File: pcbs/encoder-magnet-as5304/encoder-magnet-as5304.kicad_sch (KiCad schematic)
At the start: 14 parts, among them J1 Conn_01x05, Q1 BC807-40LWX, U1 AS5304

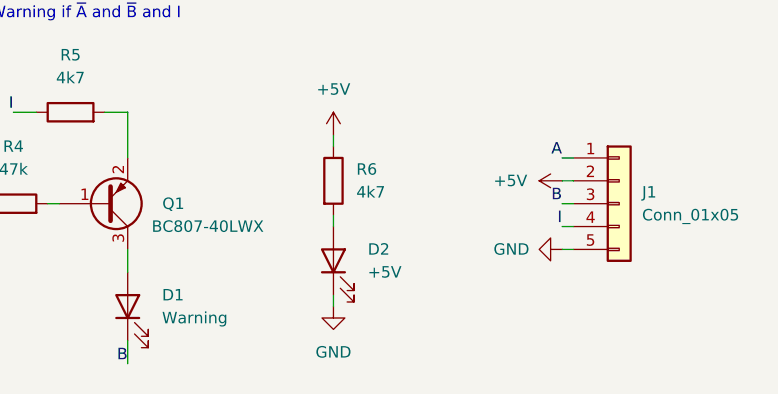
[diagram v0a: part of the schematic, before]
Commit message: Fix AS5304 board dimensions
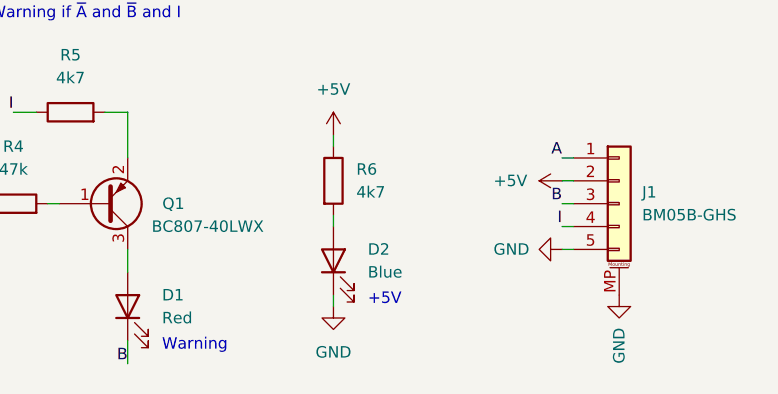
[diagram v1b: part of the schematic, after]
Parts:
- D1: value Warning -> Red
- D2: value +5V -> Blue
- J1: value Conn_01x05 -> BM05B-GHS; symbol Connector_Generic:Conn_01x05 -> Connector_Generic_MountingPin:Conn_01x05_MountingPin
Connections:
- net GND: now also J1.MP (MountPin)
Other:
- note added: "+5V"
- note added: "Warning"
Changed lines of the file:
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@@
 (kicad_sch (version 20210621) (generator eeschema)
   (paper "A4")
+  (junction (at 93.98 40.64) (diameter 0) (color 0 0 0 0))
+  (junction (at 78.74 35.56) (diameter 0) (color 0 0 0 0))
   (junction (at 86.36 38.1) (diameter 0) (color 0 0 0 0))
   (junction (at 63.5 27.94) (diameter 0) (color 0 0 0 0))
-  (junction (at 93.98 40.64) (diameter 0) (color 0 0 0 0))
-  (junction (at 78.74 35.56) (diameter 0) (color 0 0 0 0))
   (wire (pts (xy 127 54.61) (xy 127 57.15))
     (stroke (width 0) (type default) (color 0 0 0 0))
@@
     (stroke (width 0) (type default) (color 0 0 0 0))
   )
+  (wire (pts (xy 78.74 35.56) (xy 78.74 34.29))
+    (stroke (width 0) (type default) (color 0 0 0 0))
+  )
+  (wire (pts (xy 74.93 35.56) (xy 78.74 35.56))
+    (stroke (width 0) (type default) (color 0 0 0 0))
+  )
   (wire (pts (xy 78.74 35.56) (xy 80.01 35.56))
-    (stroke (width 0) (type default) (color 0 0 0 0))
-  )
-  (wire (pts (xy 78.74 35.56) (xy 78.74 34.29))
-    (stroke (width 0) (type default) (color 0 0 0 0))
-  )
-  (wire (pts (xy 74.93 35.56) (xy 78.74 35.56))
     (stroke (width 0) (type default) (color 0 0 0 0))
   )
@@
     (effects (font (size 1.27 1.27)) (justify left bottom))
   )
+  (text "Warning" (at 130.81 55.88 0)
+    (effects (font (size 1.27 1.27)) (justify left bottom))
+  )
+  (text "+5V" (at 153.67 50.8 0)
+    (effects (font (size 1.27 1.27)) (justify left bottom))
+  )
   (text "Warning if ~{A} and ~{B} and I" (at 111.76 19.05 0)
     (effects (font (size 1.27 1.27)) (justify left bottom))
@@
     (effects (font (size 1.27 1.27)) (justify right bottom))
   )
-  (symbol (lib_id "Connector_Generic:Conn_01x05") (at 181.61 39.37 0) (unit 1)
+  (symbol (lib_id "Connector_Generic_MountingPin:Conn_01x05_MountingPin") (at 181.61 39.37 0) (unit 1)
     (in_bom yes) (on_board yes) (fields_autoplaced)
     (property "Reference" "J1" (id 0) (at 184.15 38.0999 0)
       (effects (font (size 1.27 1.27)) (justify left))
     )
-    (property "Value" "Conn_01x05" (id 1) (at 184.15 40.6399 0)
+    (property "Value" "BM05B-GHS" (id 1) (at 184.15 40.6399 0)
       (effects (font (size 1.27 1.27)) (justify left))
     )
@@
     (pin "4")
     (pin "5")
+    (pin "MP")
   )
   (symbol (lib_id "Device:R") (at 149.86 36.83 0) (unit 1)
@@
     (pin "14")
     (pin "15")
-    (pin "20")
     (pin "16")
     (pin "17")
@@
     (pin "19")
     (pin "2")
+    (pin "20")
     (pin "3")
     (pin "4")
@@
       (effects (font (size 1.27 1.27)) (justify right))
     )
-    (property "Value" "+5V" (id 1) (at 153.67 46.99 90)
+    (property "Value" "Blue" (id 1) (at 153.67 46.99 90)
       (effects (font (size 1.27 1.27)) (justify right))
     )
@@
       (effects (font (size 1.27 1.27)) (justify right))
     )
-    (property "Value" "Warning" (id 1) (at 130.81 52.07 90)
+    (property "Value" "Red" (id 1) (at 130.81 52.07 90)
       (effects (font (size 1.27 1.27)) (justify right))
     )
@@
     )
     (property "Datasheet" "" (id 3) (at 25.4 44.45 0)
+      (effects (font (size 1.27 1.27)) hide)
+    )
+    (pin "1")
+  )
+  (symbol (lib_id "power:GND") (at 181.61 49.53 0) (unit 1)
+    (in_bom yes) (on_board yes)
+    (property "Reference" "#PWR?" (id 0) (at 181.61 55.88 0)
+      (effects (font (size 1.27 1.27)) hide)
+    )
+    (property "Value" "GND" (id 1) (at 181.61 57.15 90)
+      (effects (font (size 1.27 1.27)) (justify left))
+    )
+    (property "Footprint" "" (id 2) (at 181.61 49.53 0)
+      (effects (font (size 1.27 1.27)) hide)
+    )
+    (property "Datasheet" "" (id 3) (at 181.61 49.53 0)
       (effects (font (size 1.27 1.27)) hide)
     )
@@
       (reference "#PWR0113") (unit 1) (value "GND") (footprint "")
     )
+    (path "/ceb00704-4eef-40b0-a560-01e02ee946f7"
+      (reference "#PWR?") (unit 1) (value "GND") (footprint "")
+    )
     (path "/d0ad2368-a6d7-416e-b135-8689e532beca"
       (reference "C1") (unit 1) (value "100n") (footprint "Capacitor_SMD:C_0402_1005Metric")
@@
     )
     (path "/68c4efdb-d13a-4ebd-b6c5-637e69827edb"
-      (reference "D1") (unit 1) (value "Warning") (footprint "LED_SMD:LED_0402_1005Metric")
+      (reference "D1") (unit 1) (value "Red") (footprint "LED_SMD:LED_0402_1005Metric")
     )
     (path "/5bdeee7d-818b-41ff-9cc3-4ee072e480ee"
-      (reference "D2") (unit 1) (value "+5V") (footprint "LED_SMD:LED_0402_1005Metric")
+      (reference "D2") (unit 1) (value "Blue") (footprint "LED_SMD:LED_0402_1005Metric")
     )
     (path "/08520dbb-809a-40cc-84ff-87d90492eca8"
-      (reference "J1") (unit 1) (value "Conn_01x05") (footprint "Connector_JST:JST_GH_BM05B-GHS-TBT_1x05-1MP_P1.25mm_Vertical")
+      (reference "J1") (unit 1) (value "BM05B-GHS") (footprint "Connector_JST:JST_GH_BM05B-GHS-TBT_1x05-1MP_P1.25mm_Vertical")
     )
     (path "/d94d104e-7d48-4c1c-8e42-17dd90131475"
